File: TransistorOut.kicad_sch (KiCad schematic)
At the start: 45 parts, among them J1 Conn_02x15_Odd_Even, J2 OQ0412500000G, J3 OQ0412500000G, J4 OQ0412500000G, J5 TJ0411530000G, J6 TJ0411530000G, J7 TJ0411530000G, Q1 WM04N50M-CYG, Q2 WM04N50M-CYG, Q3 WM04N50M-CYG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

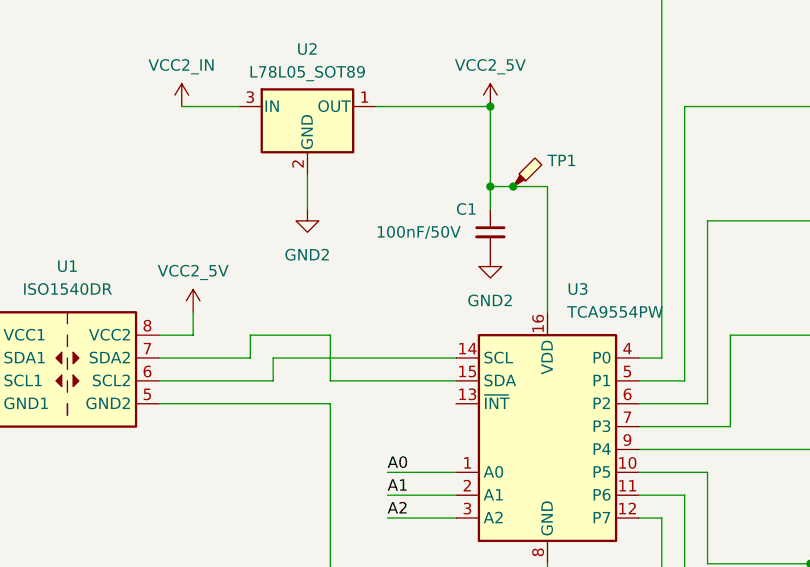
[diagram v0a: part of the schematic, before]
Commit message: dodano pullup I2C
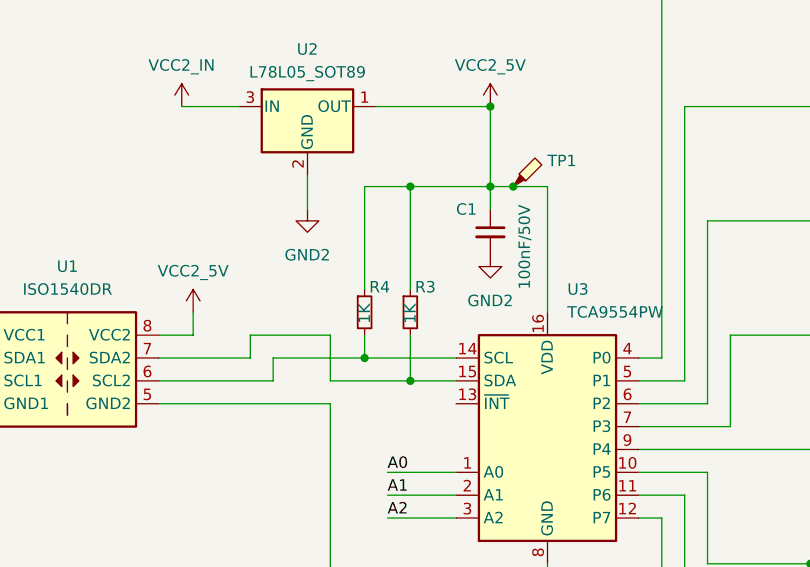
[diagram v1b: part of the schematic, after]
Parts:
- added R3, R4: 1K, Resistor_SMD:R_0603_1608Metric, symbol Device:R_Small
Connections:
- net VCC2_5V: now also R3.1, R4.1
- net at U1.6 (SCL2), U3.14 (SCL): now also R4.2
- net at U1.7 (SDA2), U3.15 (SDA): now also R3.2
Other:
- company: (none) -> KrzychoPCB
- title: (none) -> Mercury_PCB_NPNOUT_x8
